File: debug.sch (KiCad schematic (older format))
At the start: 22 parts, among them J102 10118194-0001LF, J401 Conn_01x11, J402 Conn_ARM_JTAG_SWD_10, J403 FTDI_TTL_Cable, SW401 PTS810, U103 CP2102N-A02-GQFN28R

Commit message: Added CO sensor
Carbon Monoxide Sensor layout
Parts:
- J403: symbol mylib:FTDI_TTL_Cable -> SD1-rescue:FTDI_TTL_Cable-mylib
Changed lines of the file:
@@
 	1500 6150 1500 6250
 $Comp
-L mylib:FTDI_TTL_Cable J?
+L SD1-rescue:FTDI_TTL_Cable-mylib J?
 U 1 1 5FF49A50
 P 1800 2650

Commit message: Minor cleanup
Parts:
- J403: symbol SD1-rescue:FTDI_TTL_Cable-mylib -> mylib:FTDI_TTL_Cable
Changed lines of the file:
@@
 	1500 6150 1500 6250
 $Comp
-L SD1-rescue:FTDI_TTL_Cable-mylib J?
+L mylib:FTDI_TTL_Cable J?
 U 1 1 5FF49A50
 P 1800 2650

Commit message: Minor part picking and annotation
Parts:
- J402: footprint (none) -> mylib:PinHeader_2x05_P1.27mm_Thin_Shrouded_Vertical_SMD; Digikey (none) -> SAM8799-ND; MPN (none) -> FTSH-105-01-L-DV-K; Note (none) -> 2x5 1.27mm SMD connector
- SW401: LCSC (none) -> C221897; MPN C221897 -> (none)
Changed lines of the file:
@@
 F 2 "Button_Switch_SMD:SW_SPST_PTS810" H 3450 7250 50  0001 C CNN
 F 3 "~" H 3450 7250 50  0001 C CNN
-F 4 "C221897" H 3450 7050 50  0001 C CNN "MPN"
+F 4 "" H 3450 7050 50  0001 C CNN "MPN"
 F 5 "CKN10503CT-ND" H 3450 7050 50  0001 C CNN "Digikey"
 F 6 "SWITCH TACTILE SPST-NO 0.05A 16V" H 3450 7050 50  0001 C CNN "Note"
+F 7 "C221897" H 3450 7050 50  0001 C CNN "LCSC"
 	1    3450 7050
 	0    -1   -1   0
@@
 F 0 "J402" H 1057 6850 50  0000 R CNN
 F 1 "Conn_ARM_JTAG_SWD_10" H 1057 6805 50  0001 R CNN
-F 2 "" H 1500 6850 50  0001 C CNN
+F 2 "mylib:PinHeader_2x05_P1.27mm_Thin_Shrouded_Vertical_SMD" H 1500 6850 50  0001 C CNN
 F 3 "http://infocenter.arm.com/help/topic/com.arm.doc.ddi0314h/DDI0314H_coresight_components_trm.pdf" V 1150 5600 50  0001 C CNN
+F 4 "SAM8799-ND" H 1500 6850 50  0001 C CNN "Digikey"
+F 5 "FTSH-105-01-L-DV-K" H 1500 6850 50  0001 C CNN "MPN"
+F 6 "2x5 1.27mm SMD connector" H 1500 6850 50  0001 C CNN "Note"
 	1    1500 6850
 	1    0    0    -1

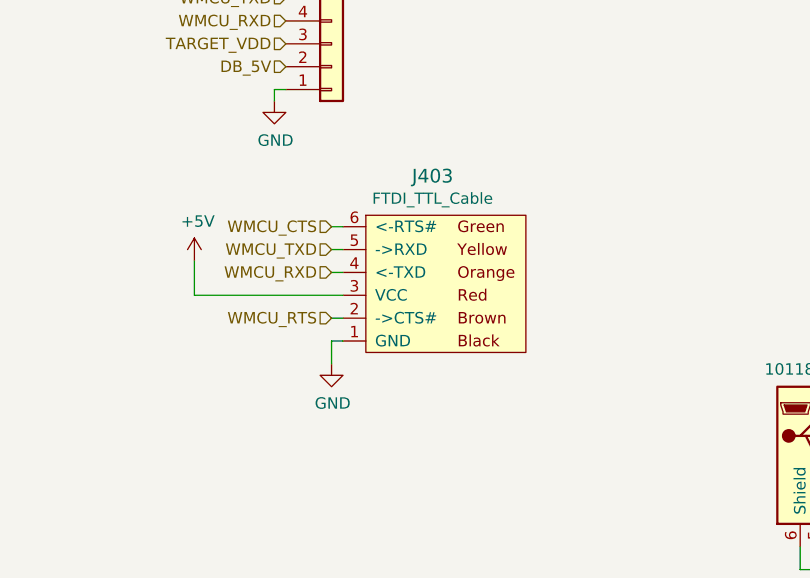
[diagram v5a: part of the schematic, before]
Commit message: Major power changes
Added 5v boost, 3.3 buck, ideal diode circuits.
Poe: added barrel jacks
Smoke: general cleanup
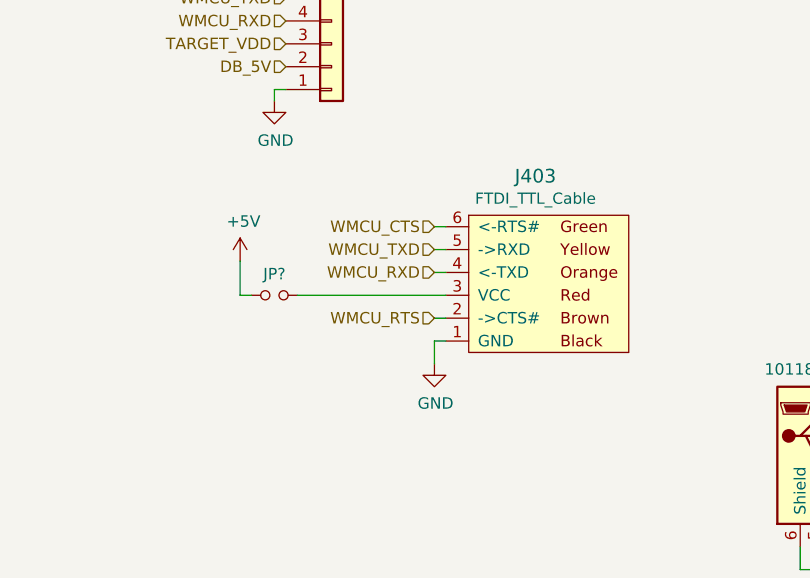
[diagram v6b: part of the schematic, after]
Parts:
- added JP?: Jumper_NO_Small, Connector_PinHeader_2.54mm:PinHeader_1x02_P2.54mm_Vertical, symbol Device:Jumper_NO_Small
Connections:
- net +5V: now also JP?.1; no longer J403.3 (VCC)
- new net: J403.3 (VCC), JP?.2
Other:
- moved on the sheet: J403
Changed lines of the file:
@@
 $Descr USLetter 11000 8500
 encoding utf-8
-Sheet 4 7
+Sheet 4 8
 Title ""
 Date ""
@@
 L mylib:FTDI_TTL_Cable J?
 U 1 1 5FF49A50
-P 1800 2650
+P 2250 2650
 AR Path="/5FF49A50" Ref="J?"  Part="1"
 AR Path="/5FED2126/5FF49A50" Ref="J403"  Part="1"
-F 0 "J403" H 1792 2179 60  0000 C CNN
-F 1 "FTDI_TTL_Cable" H 1792 2277 49  0000 C CNN
-F 2 "Connector_PinHeader_2.54mm:PinHeader_1x06_P2.54mm_Vertical" V 1800 2550 60  0001 C CNN
-F 3 "" V 1525 2725 60  0001 C CNN
-	1    1800 2650
+F 0 "J403" H 2242 2179 60  0000 C CNN
+F 1 "FTDI_TTL_Cable" H 2242 2277 49  0000 C CNN
+F 2 "Connector_PinHeader_2.54mm:PinHeader_1x06_P2.54mm_Vertical" V 2250 2550 60  0001 C CNN
+F 3 "" V 1975 2725 60  0001 C CNN
+	1    2250 2650
 	1    0    0    1
 $EndComp
@@
 L power:GND #PWR?
 U 1 1 5FF49A56
-P 1350 3000
+P 1800 3000
 AR Path="/5FF49A56" Ref="#PWR?"  Part="1"
 AR Path="/5FED2126/5FF49A56" Ref="#PWR0124"  Part="1"
-F 0 "#PWR0124" H 1350 2750 50  0001 C CNN
-F 1 "GND" H 1355 2827 50  0000 C CNN
-F 2 "" H 1350 3000 50  0001 C CNN
-F 3 "" H 1350 3000 50  0001 C CNN
-	1    1350 3000
-	1    0    0    -1
-$EndComp
-Wire Wire Line
-	1400 2900 1350 2900
-Wire Wire Line
-	1350 2900 1350 3000
-Wire Wire Line
-	1350 2800 1400 2800
-Wire Wire Line
-	1350 2400 1400 2400
-Wire Wire Line
-	1350 2500 1400 2500
-Wire Wire Line
-	1350 2600 1400 2600
+F 0 "#PWR0124" H 1800 2750 50  0001 C CNN
+F 1 "GND" H 1805 2827 50  0000 C CNN
+F 2 "" H 1800 3000 50  0001 C CNN
+F 3 "" H 1800 3000 50  0001 C CNN
+	1    1800 3000
+	1    0    0    -1
+$EndComp
+Wire Wire Line
+	1850 2900 1800 2900
+Wire Wire Line
+	1800 2900 1800 3000
+Wire Wire Line
+	1800 2800 1850 2800
+Wire Wire Line
+	1800 2400 1850 2400
+Wire Wire Line
+	1800 2500 1850 2500
+Wire Wire Line
+	1800 2600 1850 2600
 Text HLabel 1150 800  0    50   Input ~ 0
 WMCU_SWO
@@
 Text HLabel 6900 2900 2    50   Input ~ 0
 WMCU_RTS
-Text HLabel 1350 2600 0    50   Input ~ 0
+Text HLabel 1800 2600 0    50   Input ~ 0
 WMCU_RXD
-Text HLabel 1350 2500 0    50   Input ~ 0
+Text HLabel 1800 2500 0    50   Input ~ 0
 WMCU_TXD
-Text HLabel 1350 2800 0    50   Input ~ 0
+Text HLabel 1800 2800 0    50   Input ~ 0
 WMCU_RTS
-Text HLabel 1350 2400 0    50   Input ~ 0
+Text HLabel 1800 2400 0    50   Input ~ 0
 WMCU_CTS
+Wire Wire Line
+	1850 2700 1200 2700
+$Comp
+L Device:Jumper_NO_Small JP?
+U 1 1 5FCE30FC
+P 1100 2700
+F 0 "JP?" H 1100 2793 50  0000 C CNN
+F 1 "Jumper_NO_Small" H 1100 2794 50  0001 C CNN
+F 2 "Connector_PinHeader_2.54mm:PinHeader_1x02_P2.54mm_Vertical" H 1100 2700 50  0001 C CNN
+F 3 "~" H 1100 2700 50  0001 C CNN
+	1    1100 2700
+	1    0    0    -1
+$EndComp
+Wire Wire Line
+	1000 2700 950  2700
+Wire Wire Line
+	950  2700 950  2550
 $Comp
 L power:+5V #PWR?
 U 1 1 5FF49A68
-P 750 2550
+P 950 2550
 AR Path="/5FF49A68" Ref="#PWR?"  Part="1"
 AR Path="/5FED2126/5FF49A68" Ref="#PWR0180"  Part="1"
-F 0 "#PWR0180" H 750 2400 50  0001 C CNN
-F 1 "+5V" H 765 2723 50  0000 C CNN
-F 2 "" H 750 2550 50  0001 C CNN
-F 3 "" H 750 2550 50  0001 C CNN
-	1    750  2550
-	1    0    0    -1
-$EndComp
-Wire Wire Line
-	750  2700 750  2550
-Wire Wire Line
-	1400 2700 750  2700
+F 0 "#PWR0180" H 950 2400 50  0001 C CNN
+F 1 "+5V" H 965 2723 50  0000 C CNN
+F 2 "" H 950 2550 50  0001 C CNN
+F 3 "" H 950 2550 50  0001 C CNN
+	1    950  2550
+	1    0    0    -1
+$EndComp
 $EndSCHEMATC

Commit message: Continue part picking
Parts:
- D102, D103, D104: LCSC (none) -> C205443
- gave numbers to parts that had none: 1
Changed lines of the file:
@@
 F 5 "732-4978-1-ND" H 8100 4300 50  0001 C CNN "Digikey"
 F 6 "LED RED CLEAR 0603 SMD" H 8100 4300 50  0001 C CNN "Note"
+F 7 "C205443" H 8100 4300 50  0001 C CNN "LCSC"
 	1    8100 4300
 	0    -1   -1   0
@@
 F 5 "732-4978-1-ND" H 7800 4300 50  0001 C CNN "Digikey"
 F 6 "LED RED CLEAR 0603 SMD" H 7800 4300 50  0001 C CNN "Note"
+F 7 "C205443" H 7800 4300 50  0001 C CNN "LCSC"
 	1    7800 4300
 	0    -1   -1   0
@@
 F 5 "732-4978-1-ND" H 7500 4300 50  0001 C CNN "Digikey"
 F 6 "LED RED CLEAR 0603 SMD" H 7500 4300 50  0001 C CNN "Note"
+F 7 "C205443" H 7500 4300 50  0001 C CNN "LCSC"
 	1    7500 4300
 	0    -1   -1   0
@@
 	1850 2700 1200 2700
 $Comp
-L Device:Jumper_NO_Small JP?
+L Device:Jumper_NO_Small JP401
 U 1 1 5FCE30FC
 P 1100 2700
-F 0 "JP?" H 1100 2793 50  0000 C CNN
+F 0 "JP401" H 1100 2793 50  0000 C CNN
 F 1 "Jumper_NO_Small" H 1100 2794 50  0001 C CNN
 F 2 "Connector_PinHeader_2.54mm:PinHeader_1x02_P2.54mm_Vertical" H 1100 2700 50  0001 C CNN

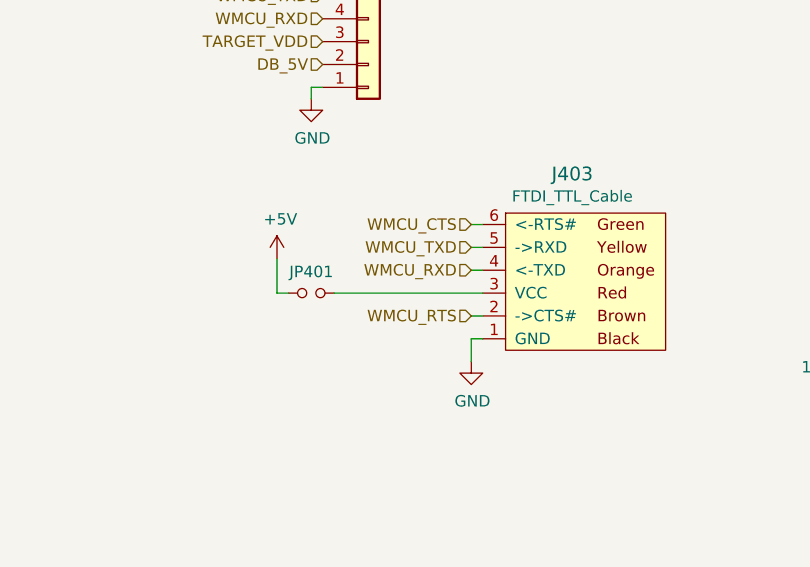
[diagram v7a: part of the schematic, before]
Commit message: Layout WIP, sch final
USB 5V Jumper works for both FTDI and microusb
Added decoupling caps for micro
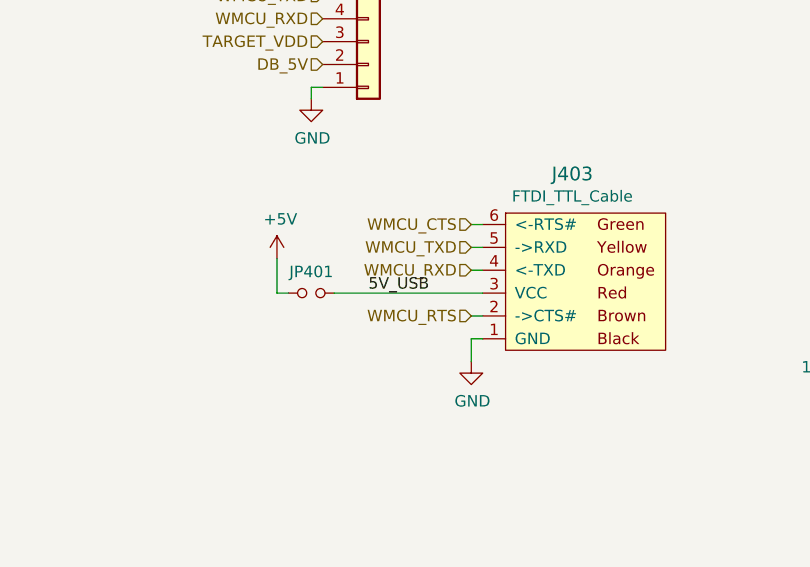
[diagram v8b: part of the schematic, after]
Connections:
- net 5V_USB: now also J403.3 (VCC), JP401.2
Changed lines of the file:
@@
 	1    0    0    -1
 $EndComp
+Text Label 1350 2700 0    50   ~ 0
+5V_USB
 $EndSCHEMATC
